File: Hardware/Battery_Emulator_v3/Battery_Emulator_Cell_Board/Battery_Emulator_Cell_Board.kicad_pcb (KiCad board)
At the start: 2 copper layers, 43.8 x 124.8 mm, 46 parts, among them J1 Conn_01x05, J3 Cell1_Vout, Q1 IRFB7545PBF, Q2 MJE2955T, Q3 MJE2955T, U1 LT3080xQ, U2 ISO1640BDR, U3 MCP4651T-103E_ST, U4 KA78M05_TO252, U5 MCP6001UT-I/OT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

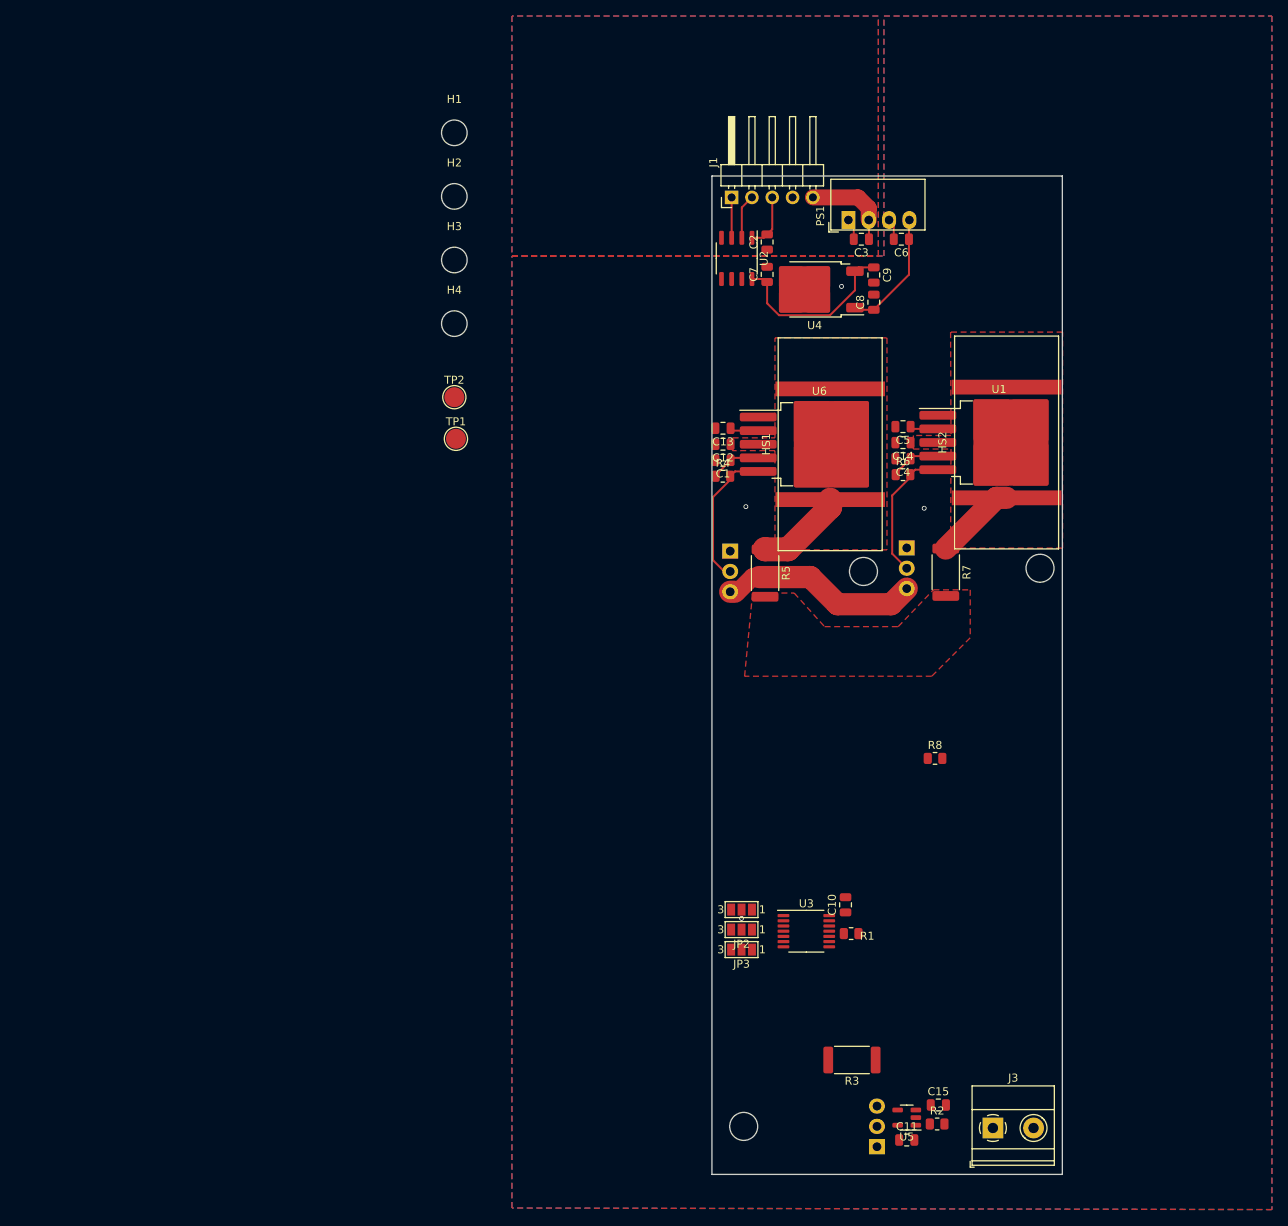
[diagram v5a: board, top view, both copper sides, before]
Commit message: Update Cell board
Finished PCB layout design.
Added two capacitors in schematic for stable feedback network for current sink.
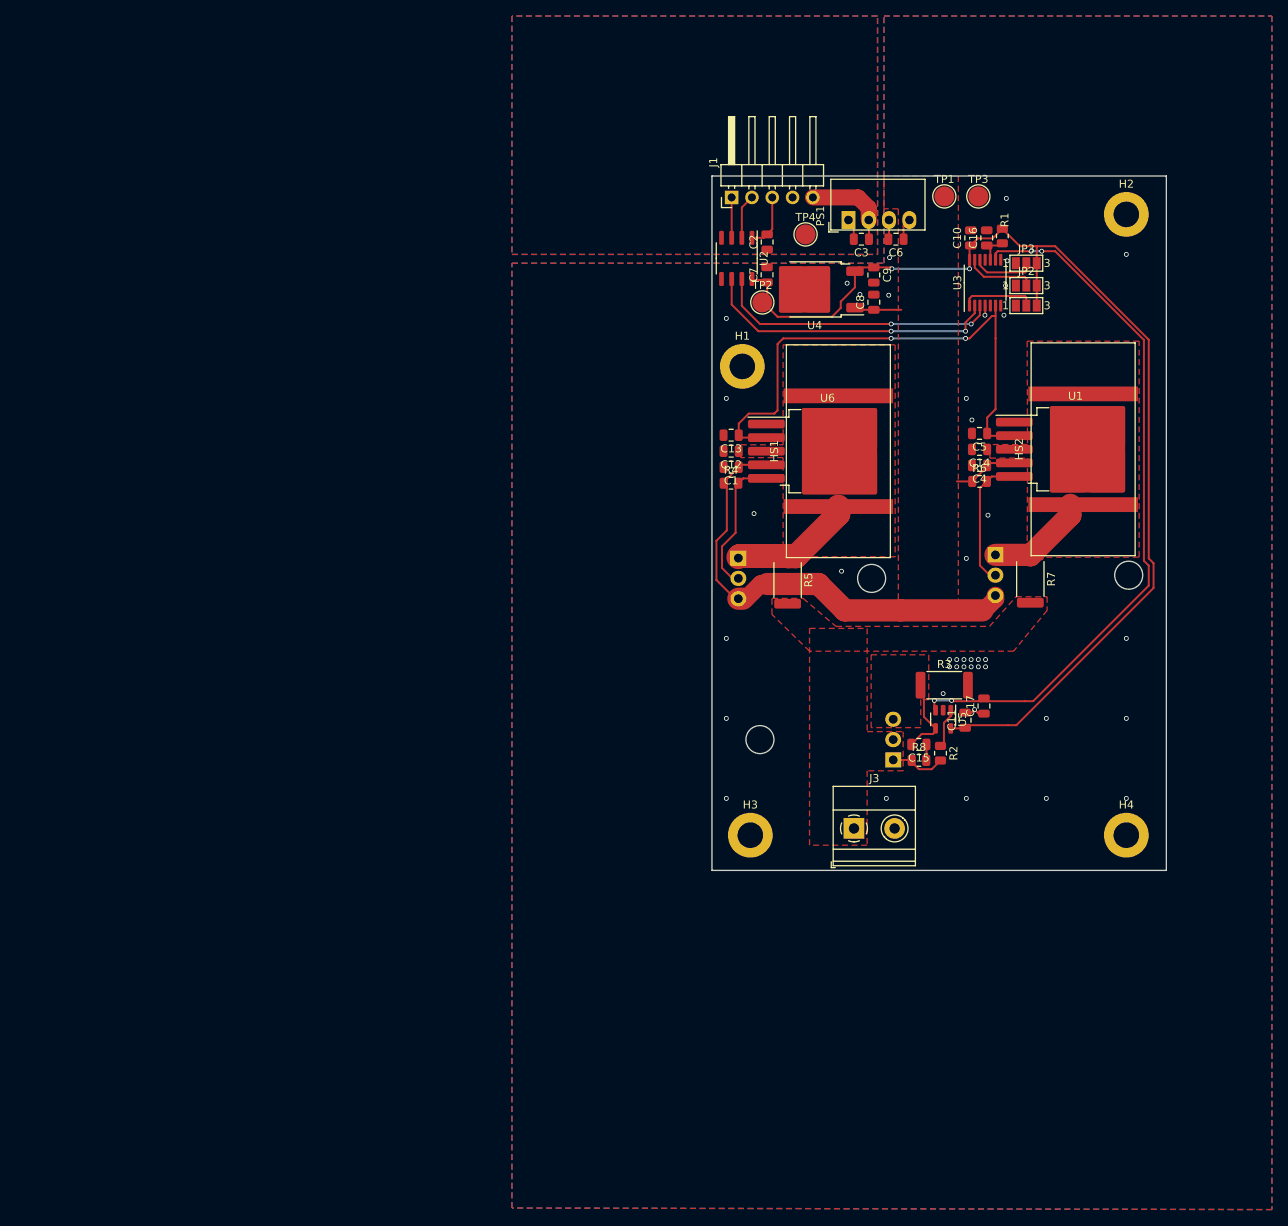
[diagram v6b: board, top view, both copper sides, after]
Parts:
- added C16: 100n, Capacitor_SMD:C_0805_2012Metric, F.Cu at (122.5, 59.9)
- added C17: 10n, Capacitor_SMD:C_0805_2012Metric, F.Cu at (122.2, 118.5)
- added TP3: GND_ISO, TestPoint:TestPoint_Pad_D2.5mm, F.Cu at (121.5, 54.8)
- added TP4: GND, TestPoint:TestPoint_Pad_D2.5mm, F.Cu at (99.9, 59.5)
- H1, H2, H3, H4: footprint MountingHole:MountingHole_3.2mm_M3 -> MountingHole:MountingHole_3.2mm_M3_DIN965_Pad
- moved H4 105.6 mm to (140.0, 134.6)
- moved JP3 92.9 mm to (127.5, 63.1), turned to 0 degrees
- moved R1 89.2 mm to (124.5, 59.7), turned to -90 degrees
- moved JP2 88.0 mm to (127.5, 65.9), turned to 0 degrees
- moved C10 84.8 mm to (120.5, 59.9)
- moved U3 84.1 mm to (122.3, 65.5), turned to 90 degrees
- moved H2 84.0 mm to (140.0, 57.0)
- moved JP1 83.5 mm to (127.5, 68.4), turned to 0 degrees
- moved H3 80.9 mm to (93.0, 134.6)
- moved TP1 68.2 mm to (117.2, 54.8)
- moved C11 53.0 mm to (119.8, 120.2), turned to 90 degrees
- moved U5 50.0 mm to (117.1, 120.1), turned to -90 degrees
- moved Q1 48.4 mm to (110.9, 125.2)
- moved R3 48.2 mm to (117.2, 115.8), turned to 0 degrees
- moved H1 46.4 mm to (92.0, 76.0)
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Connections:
- net Net-(U5A--) renamed /I_sense
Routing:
- net /+5V_ISO: track 22.5 -> 138.4 mm, vias 0 -> 2
- net Net-(U3-P0W): track 0.00 -> 89.4 mm, vias 0 -> 4
- net Net-(U1-SET): track 7.09 -> 65.9 mm, vias 0 -> 2
- net /SCL_ISO: track 0.00 -> 37.5 mm, vias 0 -> 2
- net /SDA_ISO: track 0.00 -> 35.7 mm, vias 0 -> 2
- net /+9V_ISO: track 53.2 -> 73.3 mm
- net /I_sense: track 0.00 -> 10.2 mm
- net /A0: track 0.00 -> 9.21 mm, vias 1 -> 0
- net /A1: track 0.00 -> 8.88 mm
- net /A2: track 0.00 -> 7.92 mm
- net Net-(Q1-Pad1): track 0.00 -> 6.96 mm
- net Net-(R2-Pad1): track 0.00 -> 4.99 mm
- net /OUT2_ISO: track 11.3 -> 15.7 mm
- net Net-(U3-P0B): track 0.00 -> 4.04 mm
- net /GND_ISO: track 2.64 -> 6.36 mm, vias 3 -> 42
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- added copper zone on F.Cu, net /+9V_ISO
- added copper zone on F.Cu, net /I_sense
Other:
- board size 43.8 x 124.8 mm -> 56.8 x 86.8 mm
- board text added: "JLCJLCJLCJLC"
